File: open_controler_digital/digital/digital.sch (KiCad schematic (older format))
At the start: 84 parts, among them J1 d_o_01x10, J2 d_i_01x10, J3 Conn_02x20_Odd_Even, J4 Conn_01x02, Q1 BC856, Q10 JM, Q11 JM, Q12 JM, Q2 BC856, Q3 JM, Q4 JM, Q5 BC856, Q6 BC856, Q7 BC856, Q8 BC856, Q9 JM, U1 PC817, U10 PC817, U11 PC817, U12 PC817, U2 PC817, U3 PC817, U4 PC817, U5 PC817, U6 PC817, U7 PC817, U8 PC817, U9 PC817

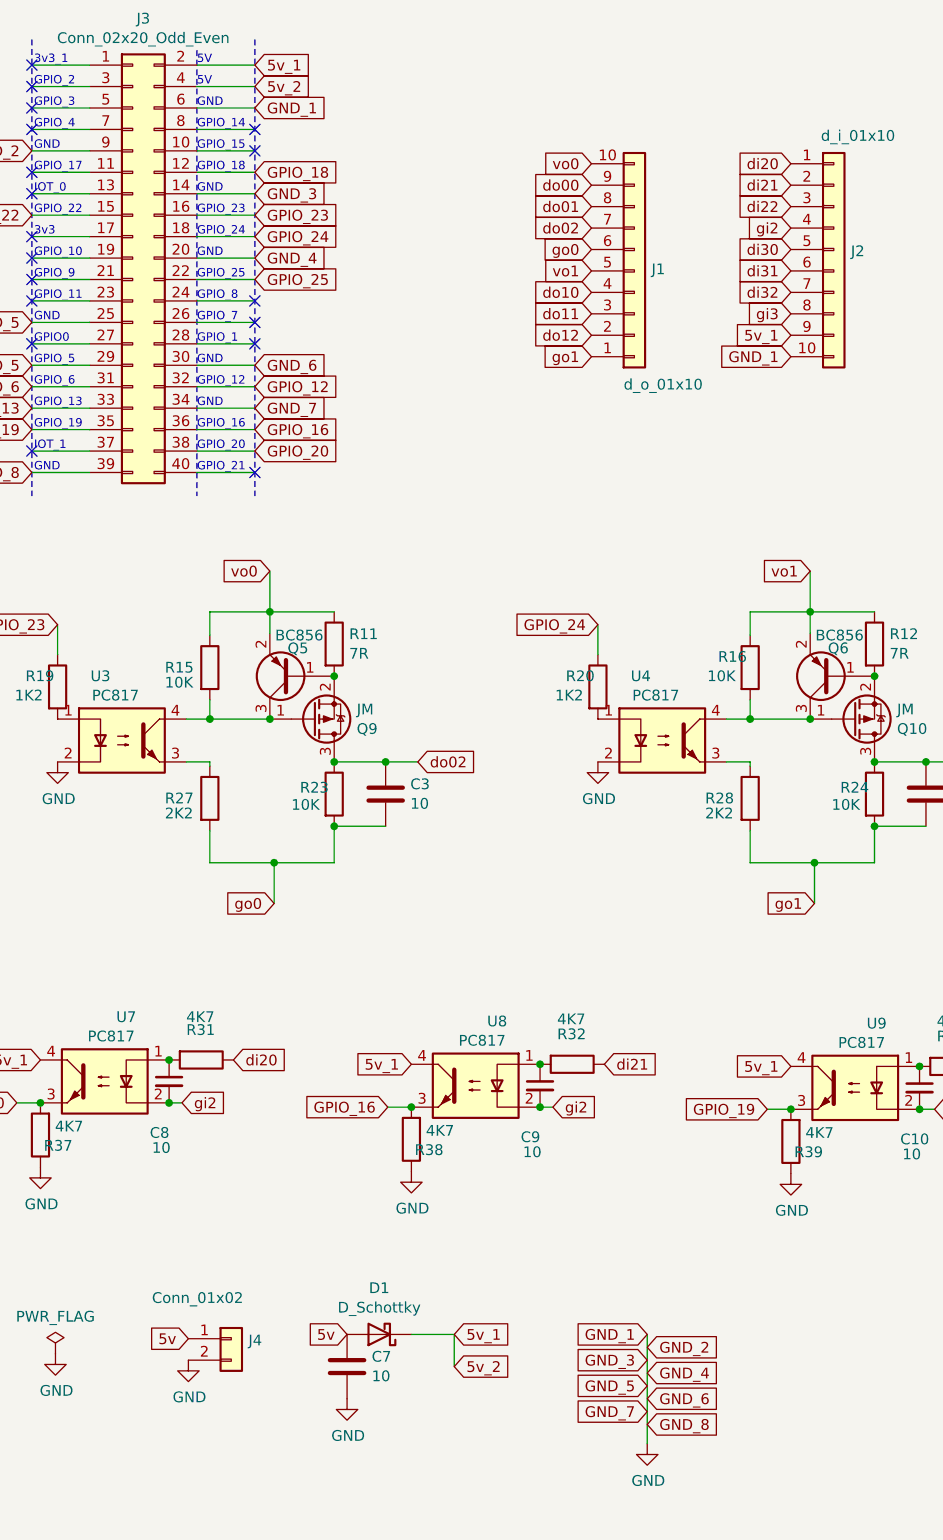
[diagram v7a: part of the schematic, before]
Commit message: digital. actualización de los conectores 3d
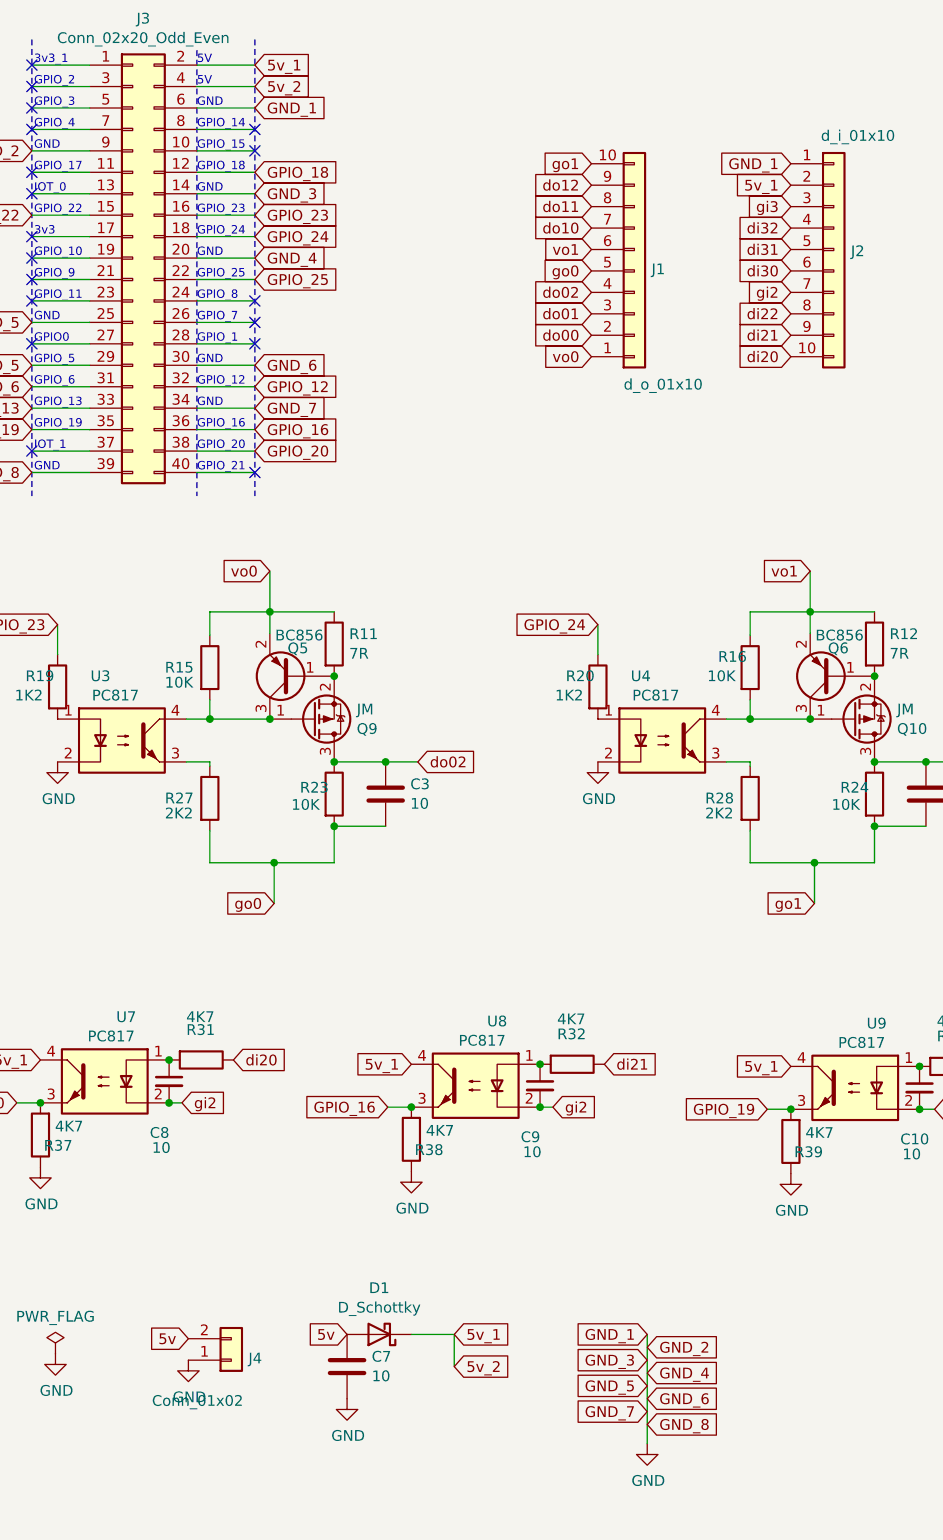
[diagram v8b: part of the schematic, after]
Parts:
- J1, J2: footprint Connector_Phoenix_MC:PhoenixContact_MCV_1,5_10-G-3.5_1x10_P3.50mm_Vertical -> Connector_Phoenix_MC:PhoenixContact_MC_1,5_10-G-3.5_1x10_P3.50mm_Horizontal
- J3: footprint Connector_PinHeader_2.54mm:PinHeader_2x20_P2.54mm_Vertical -> Connector_PinSocket_2.54mm:PinSocket_2x20_P2.54mm_Vertical
- J4: footprint Connector_Phoenix_MC:PhoenixContact_MCV_1,5_2-G-3.5_1x02_P3.50mm_Vertical -> Connector_Phoenix_MC:PhoenixContact_MC_1,5_2-G-3.5_1x02_P3.50mm_Horizontal
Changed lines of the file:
@@
 F 0 "J1" H 3980 1762 50  0000 L CNN
 F 1 "d_o_01x10" H 3850 2300 50  0000 L CNN
-F 2 "Connector_Phoenix_MC:PhoenixContact_MCV_1,5_10-G-3.5_1x10_P3.50mm_Vertical" H 3900 1770 50  0001 C CNN
+F 2 "Connector_Phoenix_MC:PhoenixContact_MC_1,5_10-G-3.5_1x10_P3.50mm_Horizontal" H 3900 1770 50  0001 C CNN
 F 3 "~" H 3900 1770 50  0001 C CNN
 	1    3900 1770
@@
 F 0 "J2" H 4910 1662 50  0000 L CNN
 F 1 "d_i_01x10" H 4770 2200 50  0000 L CNN
-F 2 "Connector_Phoenix_MC:PhoenixContact_MCV_1,5_10-G-3.5_1x10_P3.50mm_Vertical" H 4830 1670 50  0001 C CNN
+F 2 "Connector_Phoenix_MC:PhoenixContact_MC_1,5_10-G-3.5_1x10_P3.50mm_Horizontal" H 4830 1670 50  0001 C CNN
 F 3 "~" H 4830 1670 50  0001 C CNN
 	1    4830 1670
@@
 L Connector_Generic:Conn_01x02 J4
 U 1 1 622B6D5E
-P 2020 6750
-F 0 "J4" H 2100 6742 50  0000 L CNN
-F 1 "Conn_01x02" H 1650 6940 50  0000 L CNN
-F 2 "Connector_Phoenix_MC:PhoenixContact_MCV_1,5_2-G-3.5_1x02_P3.50mm_Vertical" H 2020 6750 50  0001 C CNN
-F 3 "~" H 2020 6750 50  0001 C CNN
-	1    2020 6750
-	1    0    0    -1
+P 2020 6850
+F 0 "J4" H 2100 6842 50  0000 L CNN
+F 1 "Conn_01x02" H 1650 7040 50  0000 L CNN
+F 2 "Connector_Phoenix_MC:PhoenixContact_MC_1,5_2-G-3.5_1x02_P3.50mm_Horizontal" H 2020 6850 50  0001 C CNN
+F 3 "~" H 2020 6850 50  0001 C CNN
+	1    2020 6850
+	1    0    0    1
 $EndComp
 Text GLabel 1820 6750 0    50   Input ~ 0
@@
 Text GLabel 6170 1260 0    50   Input ~ 0
 GPIO_18
-Text GLabel 3700 1370 0    50   Input ~ 0
+Text GLabel 3700 2070 0    50   Input ~ 0
 do00
-Text GLabel 3700 1470 0    50   Input ~ 0
+Text GLabel 3700 1970 0    50   Input ~ 0
 do01
 Text GLabel 2890 4060 2    50   Input ~ 0
 do02
-Text GLabel 3700 1870 0    50   Input ~ 0
+Text GLabel 3700 1570 0    50   Input ~ 0
 do10
-Text GLabel 3700 2070 0    50   Input ~ 0
+Text GLabel 3700 1370 0    50   Input ~ 0
 do12
 Text GLabel 7890 4060 2    50   Input ~ 0
 do11
-Text GLabel 4630 1270 0    50   Input ~ 0
-di20
-Text GLabel 4630 1370 0    50   Input ~ 0
-di21
-Text GLabel 4630 1470 0    50   Input ~ 0
-di22
-Text GLabel 4630 1670 0    50   Input ~ 0
-di30
-Text GLabel 4630 1870 0    50   Input ~ 0
-di32
-Text GLabel 4630 1770 0    50   Input ~ 0
-di31
+Text GLabel 3700 2170 0    50   Input ~ 0
+vo0
+Text GLabel 3700 1770 0    50   Input ~ 0
+go0
+Text GLabel 3700 1670 0    50   Input ~ 0
+vo1
 Text GLabel 3700 1270 0    50   Input ~ 0
-vo0
-Text GLabel 3700 1670 0    50   Input ~ 0
-go0
-Text GLabel 3700 1770 0    50   Input ~ 0
-vo1
-Text GLabel 3700 2170 0    50   Input ~ 0
 go1
-Text GLabel 4630 1570 0    50   Input ~ 0
-gi2
-Text GLabel 4630 1970 0    50   Input ~ 0
-gi3
 Text GLabel 1210 3420 0    50   Input ~ 0
 GPIO_23
@@
 Connection ~ 7740 4060
 Connection ~ 10190 4060
-Text GLabel 3700 1570 0    50   Input ~ 0
+Text GLabel 3700 1870 0    50   Input ~ 0
 do02
-Text GLabel 3700 1970 0    50   Input ~ 0
+Text GLabel 3700 1470 0    50   Input ~ 0
 do11
 Text GLabel 10340 4060 2    50   Input ~ 0
@@
 Text GLabel 7080 5680 2    50   Input ~ 0
 gi3
-Text GLabel 4630 2070 0    50   Input ~ 0
-5v_1
-Text GLabel 4630 2170 0    50   Input ~ 0
-GND_1
 $Comp
 L Device:D_Schottky D1
@@
 F 0 "J3" H 1610 2827 50  0000 C CNN
 F 1 "Conn_02x20_Odd_Even" H 1610 2736 50  0000 C CNN
-F 2 "Connector_PinHeader_2.54mm:PinHeader_2x20_P2.54mm_Vertical" H 1560 1710 50  0001 C CNN
+F 2 "Connector_PinSocket_2.54mm:PinSocket_2x20_P2.54mm_Vertical" H 1560 1710 50  0001 C CNN
 F 3 "~" H 1560 1710 50  0001 C CNN
 	1    1560 1710
@@
 	10350 5680 10410 5680
 Connection ~ 10350 5680
+Text GLabel 4630 1270 0    50   Input ~ 0
+GND_1
+Text GLabel 4630 1370 0    50   Input ~ 0
+5v_1
+Text GLabel 4630 1470 0    50   Input ~ 0
+gi3
+Text GLabel 4630 1870 0    50   Input ~ 0
+gi2
+Text GLabel 4630 1670 0    50   Input ~ 0
+di31
+Text GLabel 4630 1570 0    50   Input ~ 0
+di32
+Text GLabel 4630 1770 0    50   Input ~ 0
+di30
+Text GLabel 4630 1970 0    50   Input ~ 0
+di22
+Text GLabel 4630 2070 0    50   Input ~ 0
+di21
+Text GLabel 4630 2170 0    50   Input ~ 0
+di20
 $EndSCHEMATC
